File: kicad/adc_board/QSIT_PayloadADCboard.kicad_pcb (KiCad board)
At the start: 4 copper layers, 56 x 36 mm, 63 parts, among them J1 Conn_01x09, J2 Power_Conn, J4 Conn_ARM_JTAG_SWD_10, J5 UART, J6 Conn_02x05_Odd_Even, SW1 SW_Push, U1 MCP3564, U2 MAX6070, U3 STM32F373CCT6, U4 TC1108-3.3VDBTR, U5 MPE1205S-1W, X1 ECS-2520MVLC-049-BN, Y1 8MHz

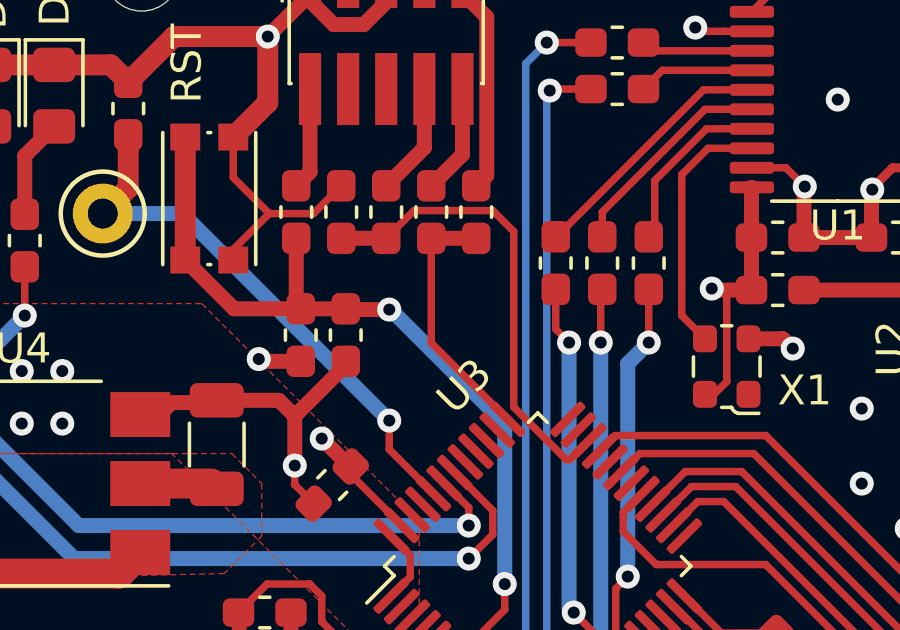
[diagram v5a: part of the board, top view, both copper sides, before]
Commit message: SWDIO/SWCLK swapped
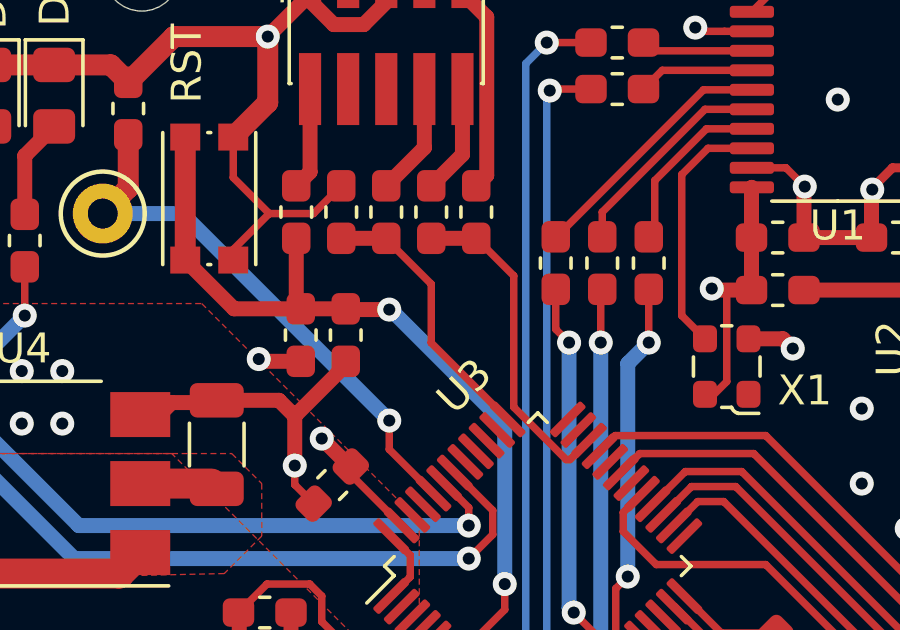
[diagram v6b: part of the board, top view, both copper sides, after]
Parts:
- J5: value UART -> Conn_01x03
- Y1: value 8MHz -> Crystal_GND24
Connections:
- R12 pad 2: SWDIO -> SWCLK
- R14 pad 1: SWDIO -> SWCLK
- R15 pad 1: SWCLK -> SWDIO
- R16 pad 2: SWCLK -> SWDIO
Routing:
- net SWDIO: track 15.8 -> 11.1 mm
- net SWCLK: track 8.59 -> 9.22 mm
